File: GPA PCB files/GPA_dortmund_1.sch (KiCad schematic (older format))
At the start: 48 parts, among them U2 ADUM4150ARIZ, U20 MC74HC1, U21 780X, U22 REF5025SOIC8, U5 ADS8684A, U6 DAC80504, U7 78L12, X2 MINI-FIT-JR-105569-NA2, X4 RJ45

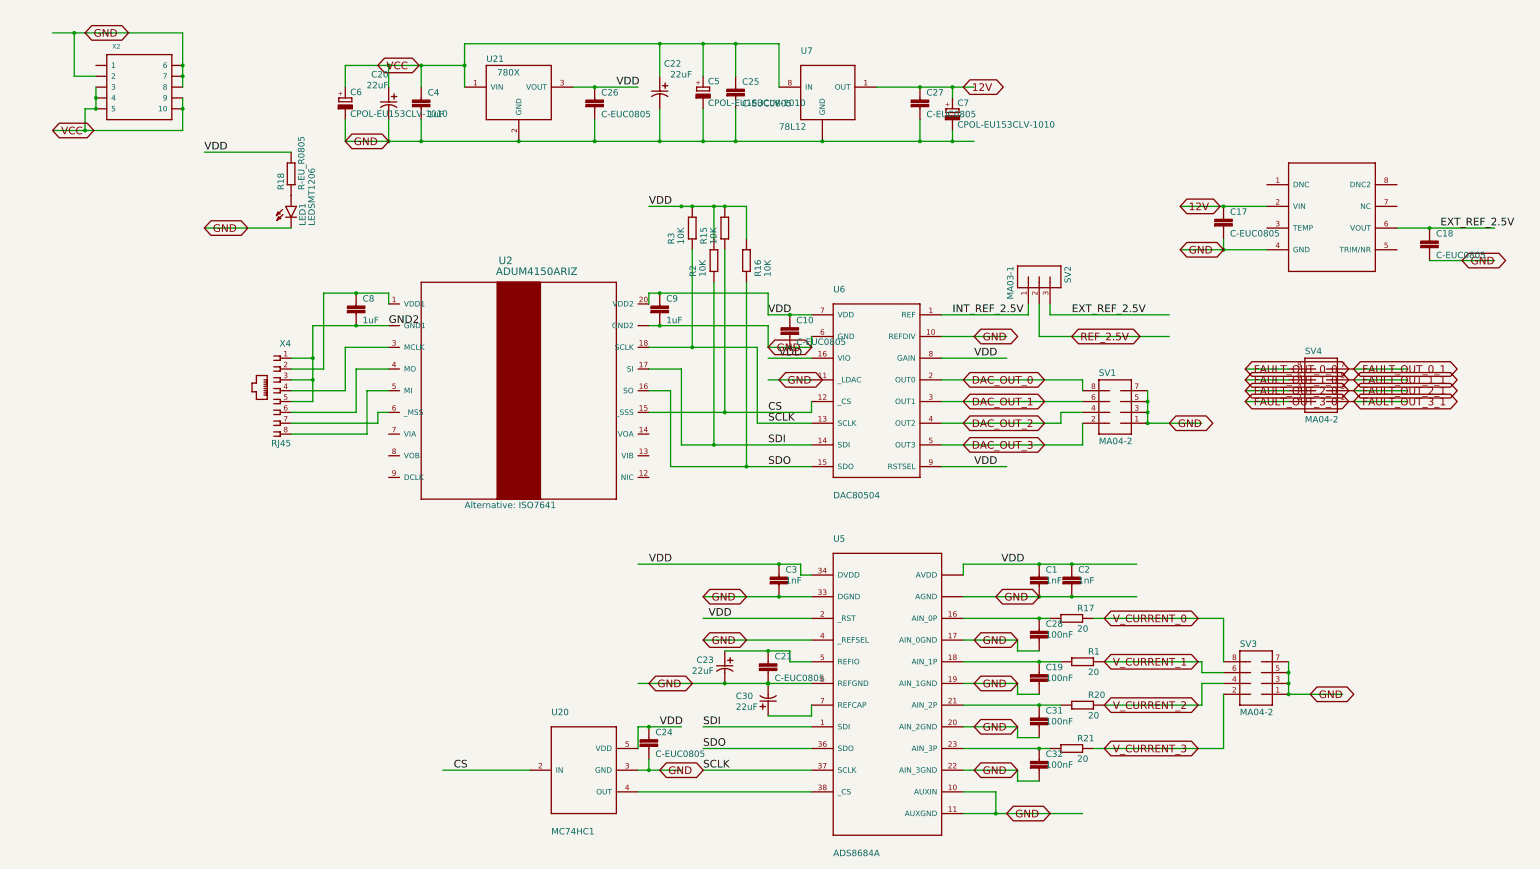
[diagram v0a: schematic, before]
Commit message: fixed schematic after conversion from eagle
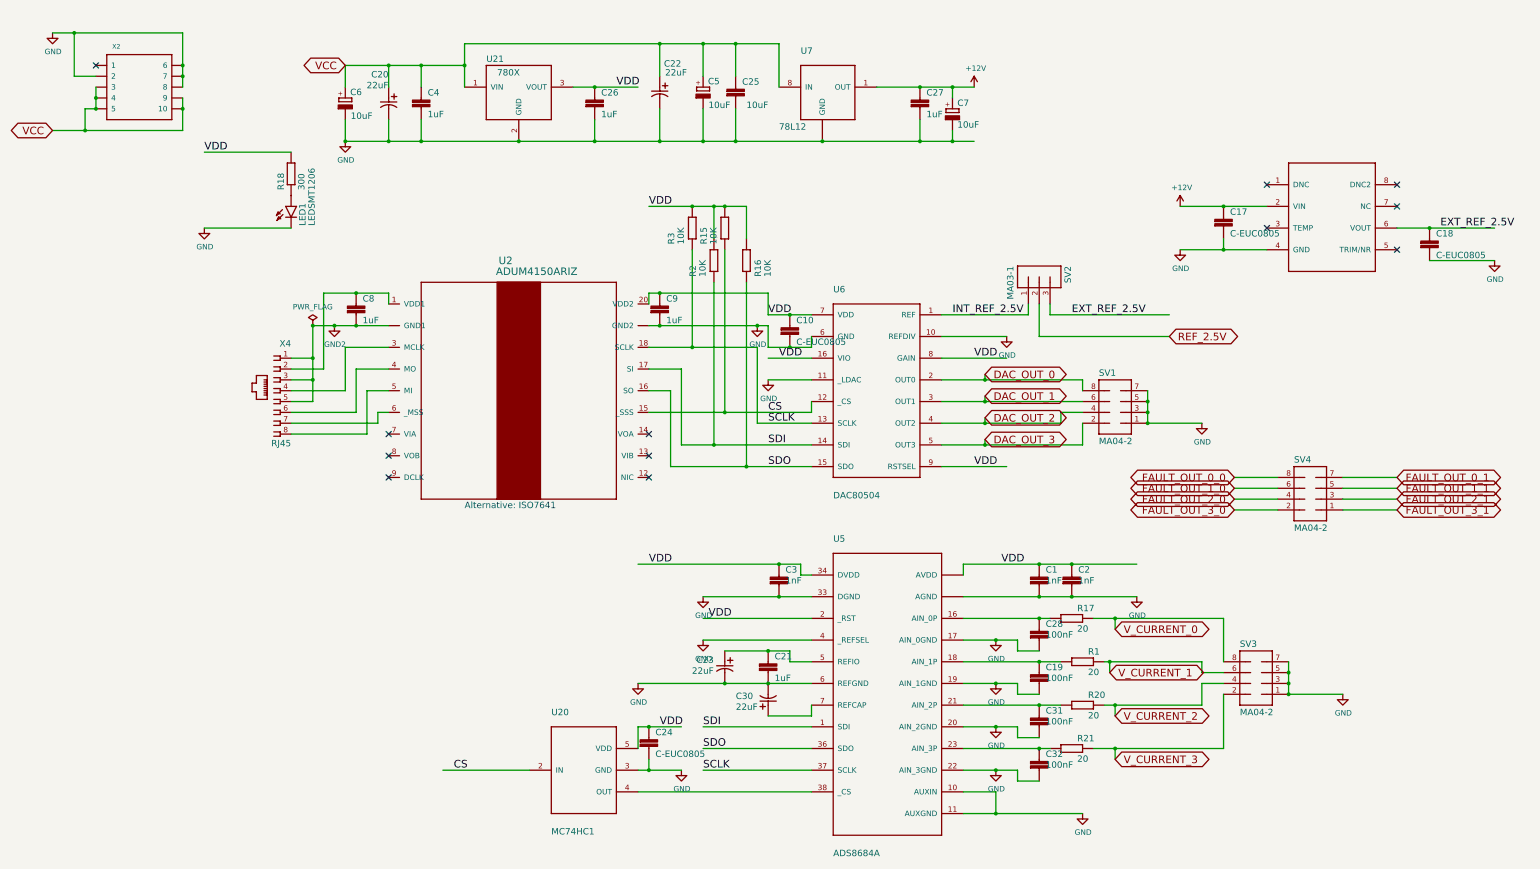
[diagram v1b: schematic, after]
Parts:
- C21, C26, C27: value C-EUC0805 -> 1uF
- C25: value C-EUC0805 -> 10uF
- C5, C6, C7: value CPOL-EU153CLV-1010 -> 10uF
- R18: value R-EU_R0805 -> 300
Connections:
- net labels added: +12V
- net labels removed: 12V
- wire segments 232 -> 255
- no-connect marks 0 -> 12
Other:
- moved on the sheet: SV4

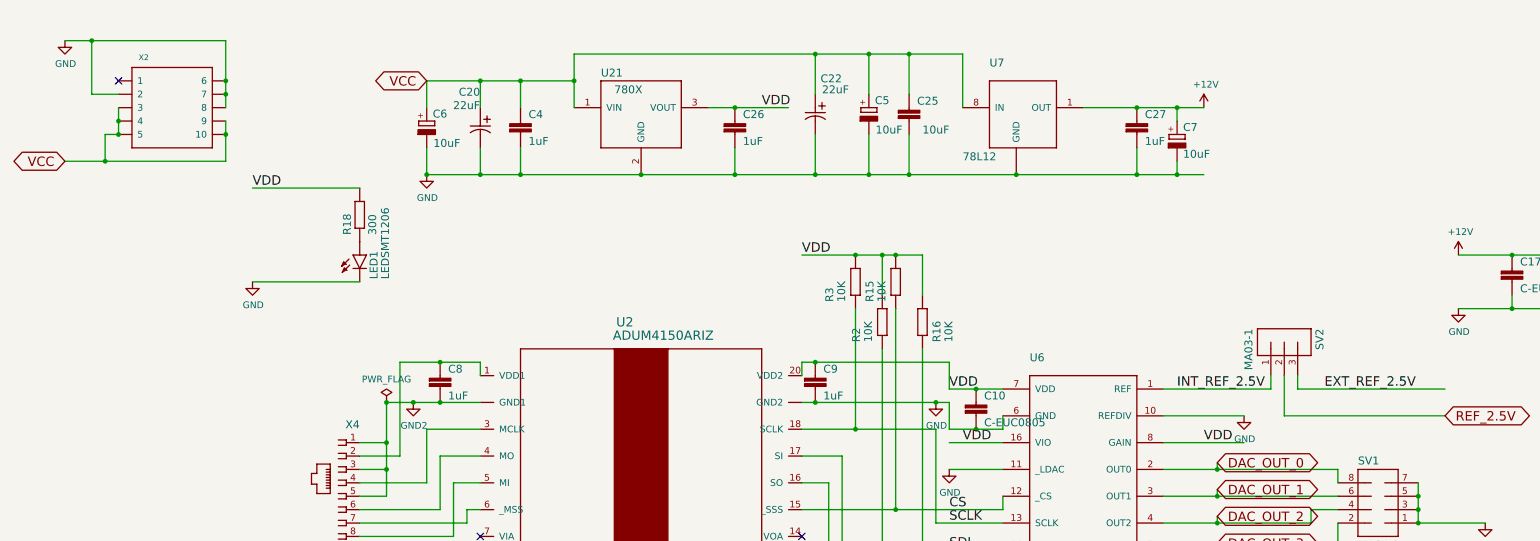
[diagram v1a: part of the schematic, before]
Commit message: more schematic fixes, only 1 ERC warning left (but thats ok)
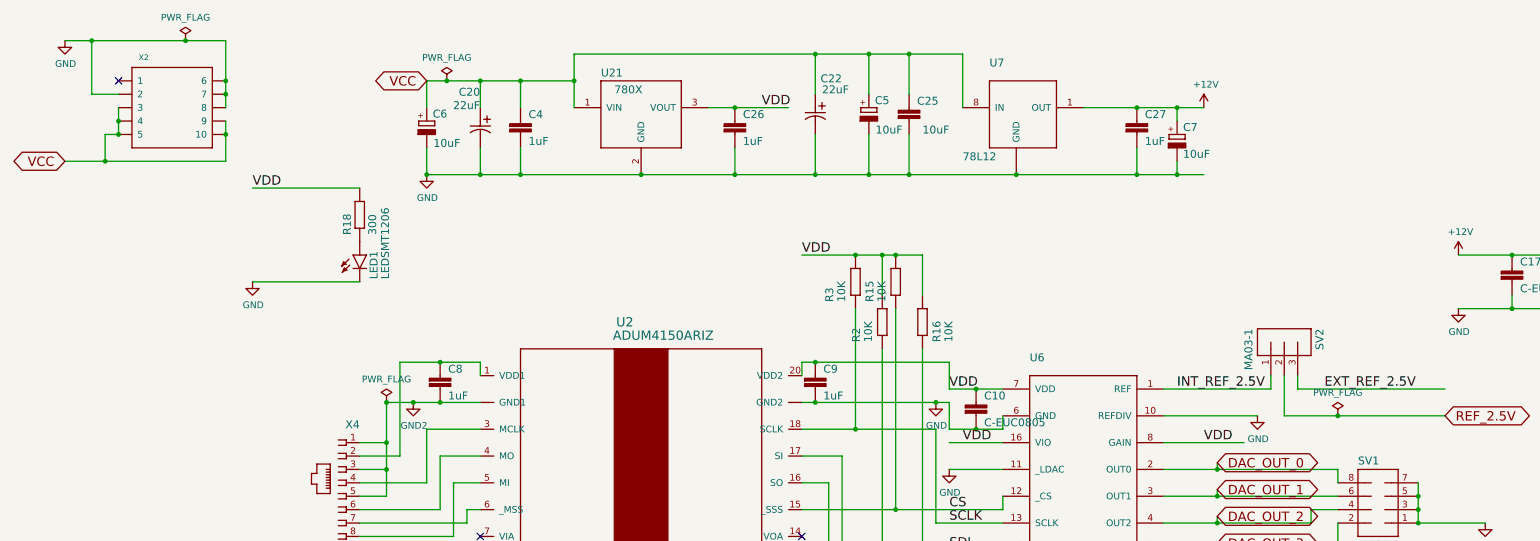
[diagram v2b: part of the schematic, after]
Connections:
- wire segments 255 -> 258
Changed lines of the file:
@@
 CS
 Wire Wire Line
-	8900 3600 9500 3600
+	8900 3600 9600 3600
 Wire Wire Line
 	3400 1800 3800 1800
@@
 	1900 1100 1900 800
 Wire Wire Line
-	1900 800  900  800
+	1900 800  1600 800
 Wire Wire Line
 	900  800  700  800
@@
 	6300 1200 6300 900
 Wire Wire Line
-	3400 1100 3800 1100
+	3400 1100 3550 1100
 Wire Wire Line
 	3800 1100 4100 1100
@@
 	9800 3300 9800 3600
 Wire Wire Line
-	9800 3600 11000 3600
+	9800 3600 10200 3600
 Text GLabel 11000 3600 2    70   BiDi ~ 0
 REF_2.5V
@@
 L power:GND #PWR0103
 U 1 1 61C71386
-P 9500 3600
-F 0 "#PWR0103" H 9500 3350 50  0001 C CNN
-F 1 "GND" H 9505 3427 50  0000 C CNN
-F 2 "" H 9500 3600 50  0001 C CNN
-F 3 "" H 9500 3600 50  0001 C CNN
-	1    9500 3600
+P 9600 3600
+F 0 "#PWR0103" H 9600 3350 50  0001 C CNN
+F 1 "GND" H 9605 3427 50  0000 C CNN
+F 2 "" H 9600 3600 50  0001 C CNN
+F 3 "" H 9600 3600 50  0001 C CNN
+	1    9600 3600
 	1    0    0    -1
 $EndComp
@@
 Wire Wire Line
 	10500 7400 11500 7400
+$Comp
+L power:PWR_FLAG #FLG0102
+U 1 1 61BAF46C
+P 10200 3600
+F 0 "#FLG0102" H 10200 3675 50  0001 C CNN
+F 1 "PWR_FLAG" H 10200 3773 50  0000 C CNN
+F 2 "" H 10200 3600 50  0001 C CNN
+F 3 "~" H 10200 3600 50  0001 C CNN
+	1    10200 3600
+	1    0    0    -1
+$EndComp
+Connection ~ 10200 3600
+Wire Wire Line
+	10200 3600 11000 3600
+$Comp
+L power:PWR_FLAG #FLG0103
+U 1 1 61C2D75B
+P 3550 1100
+F 0 "#FLG0103" H 3550 1175 50  0001 C CNN
+F 1 "PWR_FLAG" H 3550 1273 50  0000 C CNN
+F 2 "" H 3550 1100 50  0001 C CNN
+F 3 "~" H 3550 1100 50  0001 C CNN
+	1    3550 1100
+	1    0    0    -1
+$EndComp
+Connection ~ 3550 1100
+Wire Wire Line
+	3550 1100 3800 1100
+$Comp
+L power:PWR_FLAG #FLG0104
+U 1 1 61CDC7F3
+P 1600 800
+F 0 "#FLG0104" H 1600 875 50  0001 C CNN
+F 1 "PWR_FLAG" H 1600 973 50  0000 C CNN
+F 2 "" H 1600 800 50  0001 C CNN
+F 3 "~" H 1600 800 50  0001 C CNN
+	1    1600 800
+	1    0    0    -1
+$EndComp
+Connection ~ 1600 800
+Wire Wire Line
+	1600 800  900  800
 $EndSCHEMATC
